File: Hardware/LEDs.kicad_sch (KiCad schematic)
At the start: 15 parts, among them J17 ServoCH1, J18 ServoCH2, U8 PCA9685BS

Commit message: Most Review Changes
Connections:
- no-connect marks 1 -> 11
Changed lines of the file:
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@@
+	)
+	(no_connect
+		(at 211.328 90.932)
+	)
+	(no_connect
+		(at 211.328 106.172)
+	)
+	(no_connect
+		(at 211.328 85.852)
 	)
 	(no_connect
 		(at 211.328 68.072)
+	)
+	(no_connect
+		(at 211.328 96.012)
+	)
+	(no_connect
+		(at 211.328 103.632)
+	)
+	(no_connect
+		(at 211.328 93.472)
+	)
+	(no_connect
+		(at 211.328 101.092)
+	)
+	(no_connect
+		(at 211.328 88.392)
+	)
+	(no_connect
+		(at 211.328 83.312)
+	)
+	(no_connect
+		(at 211.328 98.552)
 	)
 	(wire
@@
 		)
 		(property "Value" "ORANGE_LED"
-			(at 229.87 70.612 0)
+			(at 223.52 70.612 0)
 			(effects
 				(font
@@
 		)
 		(property "Value" "PURPLE_LED"
-			(at 230.124 80.772 0)
+			(at 223.774 80.772 0)
 			(effects
 				(font
@@
 		)
 		(property "Value" "RED_LED"
-			(at 228.092 73.152 0)
+			(at 221.742 73.152 0)
 			(effects
 				(font
@@
 		)
 		(property "Value" "BLUE_LED"
-			(at 228.6 78.232 0)
+			(at 222.25 78.232 0)
 			(effects
 				(font
@@
 		)
 		(property "Value" "YELLOW_LED"
-			(at 229.87 75.692 0)
-			(effects
-				(font
+			(at 223.52 75.692 0)
+			(effects
+				(font

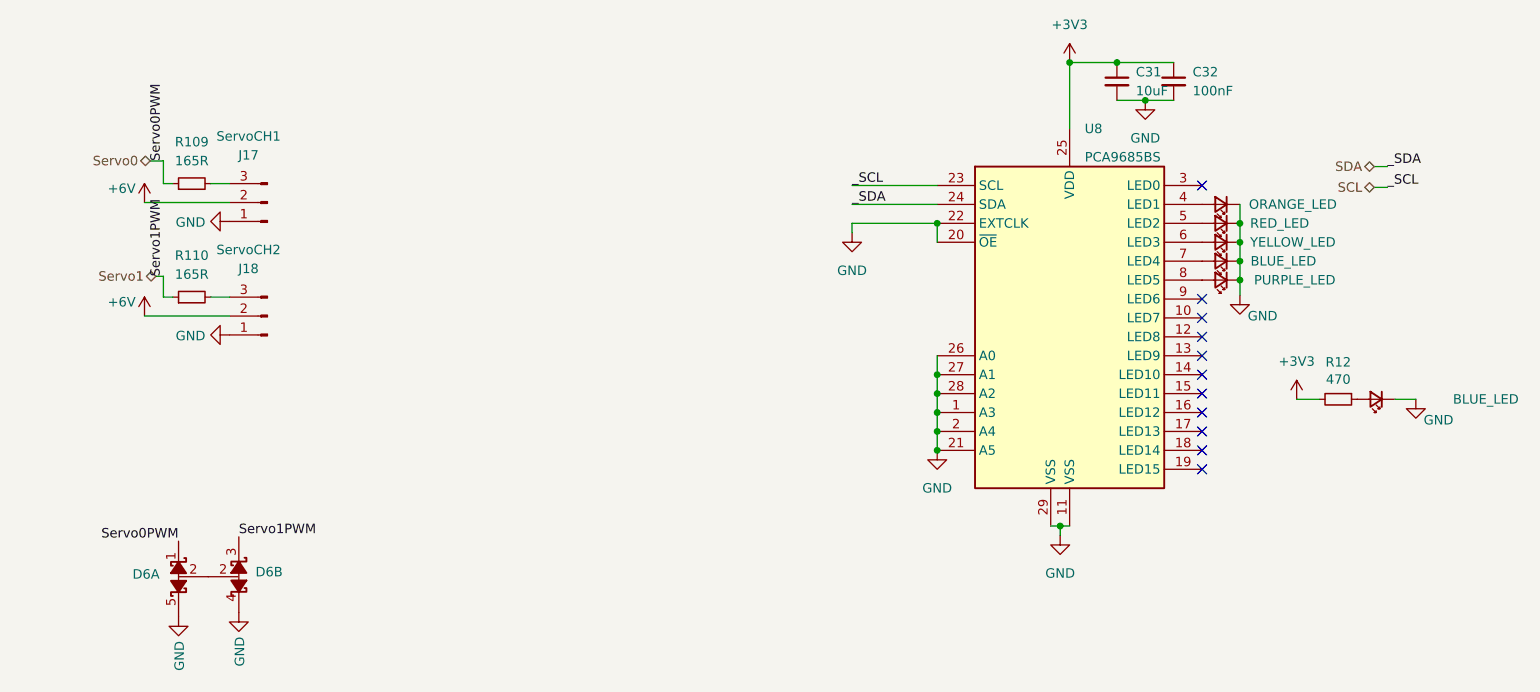
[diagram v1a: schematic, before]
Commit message: schematic reformatting and bom consolidation
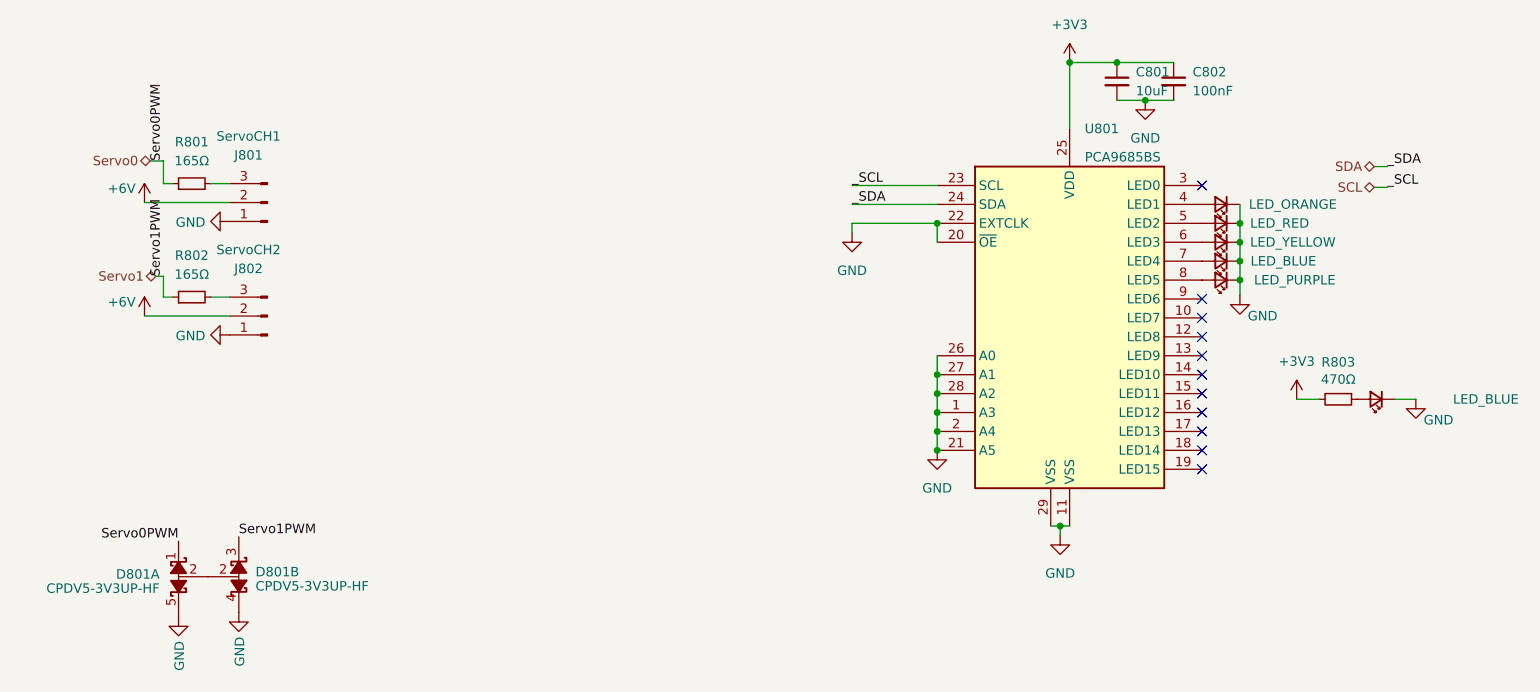
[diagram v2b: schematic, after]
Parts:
- D801: renamed from D6; value ~ -> CPDV5-3V3UP-HF
- D802: renamed from 3V3LED5; value ORANGE_LED -> LED_ORANGE
- D803: renamed from 3V3LED6; value RED_LED -> LED_RED
- D804: renamed from 3V3LED7; value YELLOW_LED -> LED_YELLOW
- D805: renamed from 3V3LED4; value BLUE_LED -> LED_BLUE
- D806: renamed from 3V3LED10; value PURPLE_LED -> LED_PURPLE
- D807: renamed from 3V3LED8; value BLUE_LED -> LED_BLUE
- R801: renamed from R109; value 165R -> 165Ω
- R802: renamed from R110; value 165R -> 165Ω
- R803: renamed from R12; value 470 -> 470Ω
- renumbered C31 to C801, C32 to C802, J17 to J801, J18 to J802, U8 to U801
